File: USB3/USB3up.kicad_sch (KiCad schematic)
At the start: 6 parts, among them Q1 NMOS

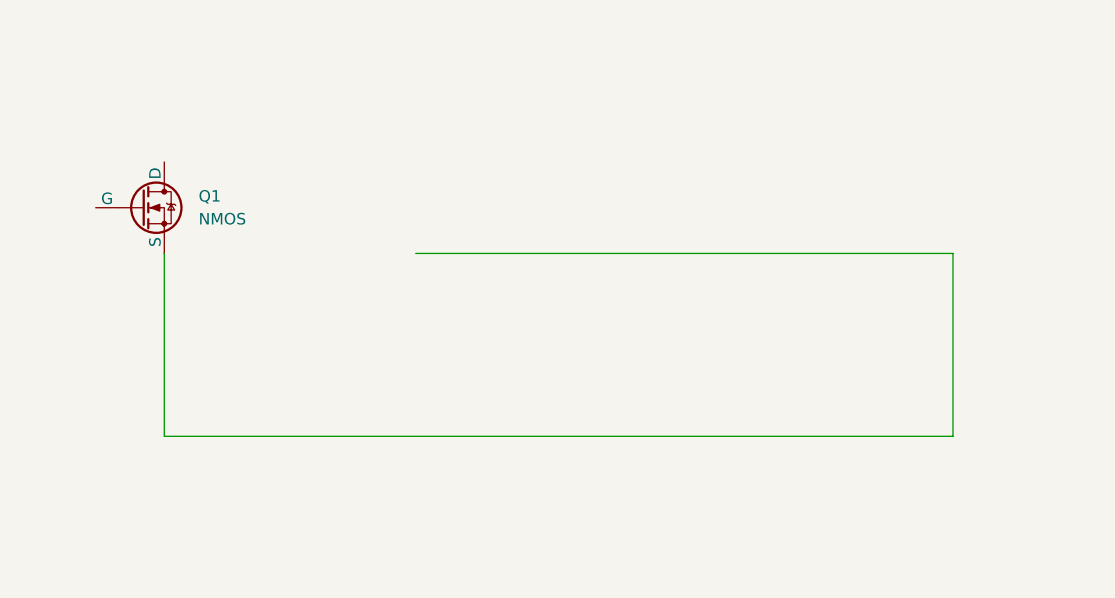
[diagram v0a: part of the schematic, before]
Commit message: added power page
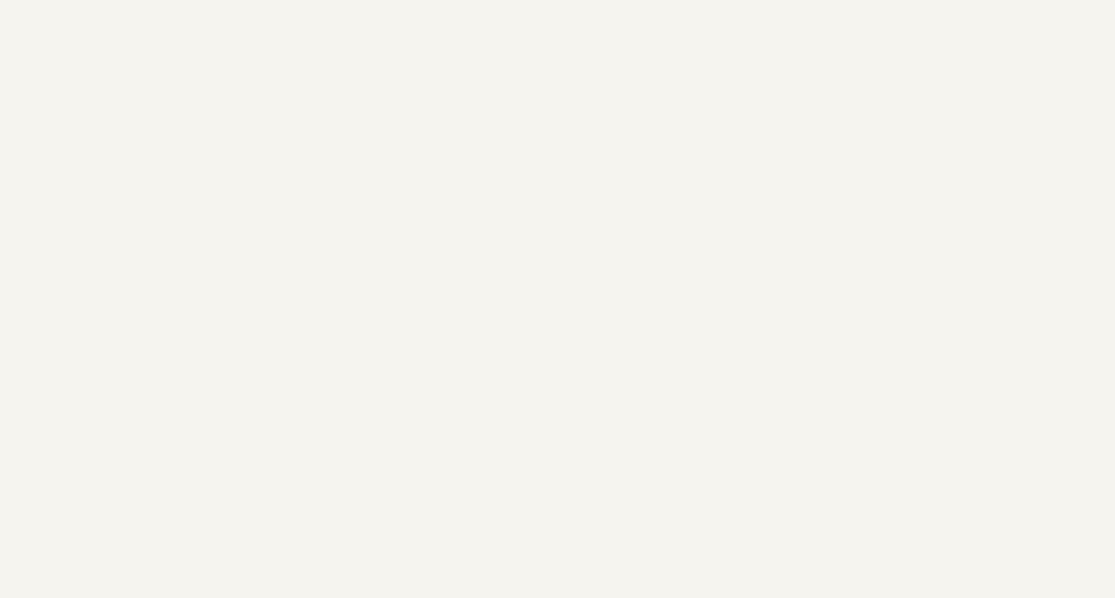
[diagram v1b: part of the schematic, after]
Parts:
- removed Q1: NMOS, symbol Simulation_SPICE:NMOS
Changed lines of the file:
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@@
-	(wire
-		(pts
-			(xy 187.96 86.36) (xy 187.96 106.68)
-		)
-		(stroke
-			(width 0)
-			(type default)
-		)
-	)
 	(wire
 		(pts
@@
 		(pts
 			(xy 274.32 133.35) (xy 274.32 132.08)
-		)
-		(stroke
-			(width 0)
-			(type default)
-		)
-	)
-	(wire
-		(pts
-			(xy 128.27 86.36) (xy 187.96 86.36)
-		)
-		(stroke
-			(width 0)
-			(type default)
-		)
-	)
-	(wire
-		(pts
-			(xy 187.96 106.68) (xy 100.33 106.68)
-		)
-		(stroke
-			(width 0)
-			(type default)
-		)
-	)
-	(wire
-		(pts
-			(xy 100.33 106.68) (xy 100.33 86.36)
 		)
 		(stroke
@@
 					(unit 1)
 				)
-			)
-		)
-	)
-	(symbol
-		(lib_id "Simulation_SPICE:NMOS")
-		(at 97.79 81.28 0)
-		(unit 1)
-		(exclude_from_sim no)
-		(in_bom yes)
-		(on_board yes)
-		(dnp no)
-		(fields_autoplaced yes)
-		(property "Reference" "Q1"
-			(at 104.14 80.0099 0)
-			(effects
-				(font
-					(size 1.27 1.27)
-				)
-				(justify left)
-			)
-		)
-		(property "Value" "NMOS"
-			(at 104.14 82.5499 0)
-			(effects
-				(font
-					(size 1.27 1.27)
-				)
-				(justify left)
-			)
-		)
-		(property "Footprint" ""
-			(at 102.87 78.74 0)
-			(effects
-				(font
-					(size 1.27 1.27)
-				)
-				(hide yes)
-			)
-		)
-		(property "Datasheet" "https://ngspice.sourceforge.io/docs/ngspice-html-manual/manual.xhtml#cha_MOSFETs"
-			(at 97.79 93.98 0)
-			(effects
-				(font
-					(size 1.27 1.27)
-				)
-				(hide yes)
-			)
-		)
-		(property "Description" "N-MOSFET transistor, drain/source/gate"
-			(at 97.79 81.28 0)
-			(effects
-				(font
-					(size 1.27 1.27)
-				)
-				(hide yes)
-			)
-		)
-		(property "Sim.Device" "NMOS"
-			(at 97.79 98.425 0)
-			(effects
-				(font
-					(size 1.27 1.27)
-				)
-				(hide yes)
-			)
-		)
-		(property "Sim.Type" "VDMOS"
-			(at 97.79 100.33 0)
-			(effects
-				(font
-					(size 1.27 1.27)
-				)
-				(hide yes)
-			)
-		)
-		(property "Sim.Pins" "1=D 2=G 3=S"
-			(at 97.79 96.52 0)
-			(effects
-				(font
-					(size 1.27 1.27)
-				)
-				(hide yes)
-			)
-		)
-		(pin "1"
-		)
-		(pin "2"
-		)
-		(pin "3"
-		)
-		(instances
-			(project ""
-				(path "/600da949-f681-489f-915b-075a1ebe377b/f20b1b5c-052b-4ece-8190-313324529590/b8f6ff93-8254-477a-8cbd-4a45901a01e5"
-					(reference "Q1")
-					(unit 1)
-				)

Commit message: merge test
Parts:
- added Q1: NMOS, symbol Simulation_SPICE:NMOS
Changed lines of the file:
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@@
+	(wire
+		(pts
+			(xy 187.96 86.36) (xy 187.96 106.68)
+		)
+		(stroke
+			(width 0)
+			(type default)
+		)
+	)
 	(wire
 		(pts
@@
 		(pts
 			(xy 274.32 133.35) (xy 274.32 132.08)
+		)
+		(stroke
+			(width 0)
+			(type default)
+		)
+	)
+	(wire
+		(pts
+			(xy 128.27 86.36) (xy 187.96 86.36)
+		)
+		(stroke
+			(width 0)
+			(type default)
+		)
+	)
+	(wire
+		(pts
+			(xy 187.96 106.68) (xy 100.33 106.68)
+		)
+		(stroke
+			(width 0)
+			(type default)
+		)
+	)
+	(wire
+		(pts
+			(xy 100.33 106.68) (xy 100.33 86.36)
 		)
 		(stroke
@@
 					(unit 1)
 				)
+			)
+		)
+	)
+	(symbol
+		(lib_id "Simulation_SPICE:NMOS")
+		(at 97.79 81.28 0)
+		(unit 1)
+		(exclude_from_sim no)
+		(in_bom yes)
+		(on_board yes)
+		(dnp no)
+		(fields_autoplaced yes)
+		(property "Reference" "Q1"
+			(at 104.14 80.0099 0)
+			(effects
+				(font
+					(size 1.27 1.27)
+				)
+				(justify left)
+			)
+		)
+		(property "Value" "NMOS"
+			(at 104.14 82.5499 0)
+			(effects
+				(font
+					(size 1.27 1.27)
+				)
+				(justify left)
+			)
+		)
+		(property "Footprint" ""
+			(at 102.87 78.74 0)
+			(effects
+				(font
+					(size 1.27 1.27)
+				)
+				(hide yes)
+			)
+		)
+		(property "Datasheet" "https://ngspice.sourceforge.io/docs/ngspice-html-manual/manual.xhtml#cha_MOSFETs"
+			(at 97.79 93.98 0)
+			(effects
+				(font
+					(size 1.27 1.27)
+				)
+				(hide yes)
+			)
+		)
+		(property "Description" "N-MOSFET transistor, drain/source/gate"
+			(at 97.79 81.28 0)
+			(effects
+				(font
+					(size 1.27 1.27)
+				)
+				(hide yes)
+			)
+		)
+		(property "Sim.Device" "NMOS"
+			(at 97.79 98.425 0)
+			(effects
+				(font
+					(size 1.27 1.27)
+				)
+				(hide yes)
+			)
+		)
+		(property "Sim.Type" "VDMOS"
+			(at 97.79 100.33 0)
+			(effects
+				(font
+					(size 1.27 1.27)
+				)
+				(hide yes)
+			)
+		)
+		(property "Sim.Pins" "1=D 2=G 3=S"
+			(at 97.79 96.52 0)
+			(effects
+				(font
+					(size 1.27 1.27)
+				)
+				(hide yes)
+			)
+		)
+		(pin "1"
+		)
+		(pin "2"
+		)
+		(pin "3"
+		)
+		(instances
+			(project ""
+				(path "/600da949-f681-489f-915b-075a1ebe377b/f20b1b5c-052b-4ece-8190-313324529590/b8f6ff93-8254-477a-8cbd-4a45901a01e5"
+					(reference "Q1")
+					(unit 1)
+				)
